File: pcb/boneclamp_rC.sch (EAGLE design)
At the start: 133 parts, among them U1 OPA365AIDBVR, U10 AD5686, U11 LM2663, U12 MAX1735, U13 TLV70245, U14 REF5040, U15 AD8032, U16 24C, U2 OPA365AIDBVR, U3 OPA365AIDBVR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

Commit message: Working on mixed signal ICs/
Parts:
- added SJ2: (no value), jumper:SJ
- R36: device boneclamp:TRIM_US- -> boneclamp:TRIM_US-M84W
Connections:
- new net N$28: BB1.GND@7, SJ2.1
- new net PE: SJ2.2
- net ADC_SPI0: now also BB1.GPIO1_1
- net ADC_SPI1: now also BB1.GPIO1_4
- net ADC_SPI2: now also BB1.GPIO1_5
- net ADC_SPI3: now also BB1.GPIO1_30
- net ADC_SPI4: now also BB1.GPIO1_31
- net DAC_SPI0: now also BB1.GPIO1_14
- net DAC_SPI1: now also BB1.GPIO1_15
- net DAC_SPI2: now also BB1.GPIO1_12
- net DGND: no longer RESET.S
- net ~RST: no longer RESET.P
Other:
- moved on the sheet: R24, R25
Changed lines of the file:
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@@
 <part name="SUPPLY21" library="supply2" deviceset="AGND" device=""/>
 <part name="VBIAS" library="testpad" deviceset="TP" device="B1,27"/>
-<part name="R36" library="boneclamp" deviceset="TRIM_US-" device="" value="10k"/>
+<part name="R36" library="boneclamp" deviceset="TRIM_US-" device="M84W" value="10k"/>
 <part name="C42" library="rcl" deviceset="C-EU" device="C0603" value="0.1uF"/>
 <part name="SUPPLY13" library="supply2" deviceset="AGND" device=""/>
@@
 <part name="R14" library="rcl" deviceset="R-US_" device="R0603" value="10"/>
 <part name="C38" library="rcl" deviceset="C-US" device="C1206" value="4.7uF"/>
+<part name="SJ2" library="jumper" deviceset="SJ" device=""/>
 </parts>
 <sheets>
@@
 <instances>
 <instance part="BB1" gate="G$1" x="-35.56" y="48.26"/>
-<instance part="DGND2" gate="PE" x="2.54" y="-20.32"/>
+<instance part="DGND2" gate="PE" x="-86.36" y="104.14" rot="MR0"/>
 <instance part="SUPPLY8" gate="G$1" x="17.78" y="33.02"/>
 <instance part="A_I/O" gate="G$1" x="53.34" y="30.48"/>
@@
 <instance part="RESET" gate="G$1" x="81.28" y="7.62" rot="R270"/>
 <instance part="DGND10" gate="PE" x="93.98" y="0"/>
+<instance part="SJ2" gate="1" x="-78.74" y="109.22" rot="MR0"/>
 </instances>
 <busses>
@@
 <net name="DGND" class="0">
 <segment>
-<pinref part="RESET" gate="G$1" pin="S"/>
 <pinref part="RESET" gate="G$1" pin="S1"/>
-<wire x1="86.36" y1="7.62" x2="86.36" y2="5.08" width="0.1524" layer="91"/>
 <wire x1="86.36" y1="5.08" x2="93.98" y2="5.08" width="0.1524" layer="91"/>
-<junction x="86.36" y="5.08"/>
 <pinref part="DGND10" gate="PE" pin="PE"/>
 <wire x1="93.98" y1="2.54" x2="93.98" y2="5.08" width="0.1524" layer="91"/>
@@
 <label x="27.94" y="73.66" size="1.778" layer="95"/>
 </segment>
+<segment>
+<pinref part="BB1" gate="G$1" pin="GPIO1_1"/>
+<wire x1="-7.62" y1="81.28" x2="10.16" y2="81.28" width="0.1524" layer="91"/>
+<wire x1="-7.62" y1="81.28" x2="10.16" y2="81.28" width="0.1524" layer="91"/>
+</segment>
 </net>
 <net name="ADC_SPI1" class="0">
@@
 <label x="27.94" y="71.12" size="1.778" layer="95"/>
 </segment>
+<segment>
+<pinref part="BB1" gate="G$1" pin="GPIO1_4"/>
+<wire x1="-63.5" y1="81.28" x2="-81.28" y2="81.28" width="0.1524" layer="91"/>
+</segment>
 </net>
 <net name="ADC_SPI2" class="0">
@@
 <label x="27.94" y="68.58" size="1.778" layer="95"/>
 </segment>
+<segment>
+<pinref part="BB1" gate="G$1" pin="GPIO1_5"/>
+<wire x1="-7.62" y1="83.82" x2="10.16" y2="83.82" width="0.1524" layer="91"/>
+</segment>
 </net>
 <net name="ADC_SPI3" class="0">
@@
 <label x="27.94" y="66.04" size="1.778" layer="95"/>
 </segment>
+<segment>
+<pinref part="BB1" gate="G$1" pin="GPIO1_30"/>
+<wire x1="-63.5" y1="83.82" x2="-81.28" y2="83.82" width="0.1524" layer="91"/>
+</segment>
 </net>
 <net name="ADC_SPI4" class="0">
@@
 <label x="27.94" y="63.5" size="1.778" layer="95"/>
 </segment>
+<segment>
+<pinref part="BB1" gate="G$1" pin="GPIO1_31"/>
+<wire x1="-7.62" y1="86.36" x2="10.16" y2="86.36" width="0.1524" layer="91"/>
+</segment>
 </net>
 <net name="DAC_SPI0" class="0">
@@
 <label x="76.2" y="73.66" size="1.778" layer="95"/>
 </segment>
+<segment>
+<pinref part="BB1" gate="G$1" pin="GPIO1_14"/>
+<wire x1="-7.62" y1="91.44" x2="10.16" y2="91.44" width="0.1524" layer="91"/>
+</segment>
 </net>
 <net name="DAC_SPI1" class="0">
@@
 <label x="76.2" y="71.12" size="1.778" layer="95"/>
 </segment>
+<segment>
+<pinref part="BB1" gate="G$1" pin="GPIO1_15"/>
+<wire x1="-63.5" y1="91.44" x2="-81.28" y2="91.44" width="0.1524" layer="91"/>
+</segment>
 </net>
 <net name="DAC_SPI2" class="0">
@@
 <label x="76.2" y="68.58" size="1.778" layer="95"/>
 </segment>
+<segment>
+<pinref part="BB1" gate="G$1" pin="GPIO1_12"/>
+<wire x1="-7.62" y1="96.52" x2="10.16" y2="96.52" width="0.1524" layer="91"/>
+</segment>
 </net>
 <net name="~RST" class="0">
 <segment>
-<pinref part="RESET" gate="G$1" pin="P"/>
 <pinref part="RESET" gate="G$1" pin="P1"/>
-<wire x1="76.2" y1="7.62" x2="76.2" y2="5.08" width="0.1524" layer="91"/>
 <wire x1="76.2" y1="5.08" x2="66.04" y2="5.08" width="0.1524" layer="91"/>
-<junction x="76.2" y="5.08"/>
 <label x="66.04" y="5.08" size="1.778" layer="95"/>
 </segment>
@@
 <wire x1="35.56" y1="5.08" x2="50.8" y2="5.08" width="0.1524" layer="91"/>
 <label x="35.56" y="5.08" size="1.778" layer="95"/>
+</segment>
+</net>
+<net name="N$28" class="0">
+<segment>
+<pinref part="BB1" gate="G$1" pin="GND@7"/>
+<wire x1="-63.5" y1="109.22" x2="-73.66" y2="109.22" width="0.1524" layer="91"/>
+<pinref part="SJ2" gate="1" pin="1"/>
+</segment>
+</net>
+<net name="PE" class="0">
+<segment>
+<pinref part="DGND2" gate="PE" pin="PE"/>
+<wire x1="-86.36" y1="109.22" x2="-86.36" y2="106.68" width="0.1524" layer="91"/>
+<pinref part="SJ2" gate="1" pin="2"/>
+<wire x1="-83.82" y1="109.22" x2="-86.36" y2="109.22" width="0.1524" layer="91"/>
 </segment>
 </net>
@@
 <instance part="C24" gate="G$1" x="25.4" y="10.16"/>
 <instance part="SUPPLY7" gate="G$1" x="25.4" y="-2.54"/>
-<instance part="R24" gate="G$1" x="-50.8" y="-20.32" rot="R270"/>
-<instance part="R25" gate="G$1" x="-43.18" y="-20.32" rot="R270"/>
+<instance part="R24" gate="G$1" x="-50.8" y="12.7" rot="MR90"/>
+<instance part="R25" gate="G$1" x="-43.18" y="12.7" rot="MR90"/>
 <instance part="U6" gate="A" x="0" y="144.78"/>
 <instance part="R15" gate="G$1" x="-40.64" y="139.7" rot="R180"/>
@@
 <segment>
 <pinref part="R24" gate="G$1" pin="2"/>
-<wire x1="-50.8" y1="-25.4" x2="-50.8" y2="-33.02" width="0.1524" layer="91"/>
+<wire x1="-50.8" y1="17.78" x2="-50.8" y2="22.86" width="0.1524" layer="91"/>
 <pinref part="R25" gate="G$1" pin="2"/>
-<wire x1="-43.18" y1="-25.4" x2="-43.18" y2="-33.02" width="0.1524" layer="91"/>
-<wire x1="-50.8" y1="-33.02" x2="-43.18" y2="-33.02" width="0.1524" layer="91"/>
-<wire x1="-43.18" y1="-33.02" x2="-43.18" y2="-43.18" width="0.1524" layer="91"/>
-<junction x="-43.18" y="-33.02"/>
-<wire x1="-43.18" y1="-43.18" x2="-55.88" y2="-43.18" width="0.1524" layer="91"/>
-<label x="-55.88" y="-43.18" size="1.778" layer="95"/>
+<wire x1="-43.18" y1="17.78" x2="-43.18" y2="22.86" width="0.1524" layer="91"/>
+<wire x1="-50.8" y1="22.86" x2="-43.18" y2="22.86" width="0.1524" layer="91"/>
+<wire x1="-50.8" y1="22.86" x2="-88.9" y2="22.86" width="0.1524" layer="91"/>
+<junction x="-50.8" y="22.86"/>
+<label x="-88.9" y="22.86" size="1.778" layer="95"/>
 </segment>
 </net>
@@
 <pinref part="R24" gate="G$1" pin="1"/>
 <wire x1="-50.8" y1="2.54" x2="-88.9" y2="2.54" width="0.1524" layer="91"/>
-<wire x1="-50.8" y1="-15.24" x2="-50.8" y2="2.54" width="0.1524" layer="91"/>
+<wire x1="-50.8" y1="7.62" x2="-50.8" y2="2.54" width="0.1524" layer="91"/>
 <junction x="-50.8" y="2.54"/>
 <label x="-88.9" y="2.54" size="1.778" layer="95"/>
@@
 <segment>
 <pinref part="R25" gate="G$1" pin="1"/>
-<wire x1="-43.18" y1="-15.24" x2="-43.18" y2="0" width="0.1524" layer="91"/>
+<wire x1="-43.18" y1="7.62" x2="-43.18" y2="0" width="0.1524" layer="91"/>
 <pinref part="U10" gate="G$1" pin="LDAC*"/>
 <wire x1="-88.9" y1="0" x2="-43.18" y2="0" width="0.1524" layer="91"/>

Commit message: Fixed the ground planes.
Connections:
- removed net N$28: BB1.GND@7, SJ2.1
- removed net PE: SJ2.2
- new net N$8: BB1.GND@2, SJ2.1
- net AGND: now also BB1.GND@1; no longer BB1.GND@2
- net DGND: now also SJ2.2
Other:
- moved on the sheet: SJ2
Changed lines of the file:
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@@
 <instances>
 <instance part="BB1" gate="G$1" x="-35.56" y="48.26"/>
-<instance part="DGND2" gate="PE" x="-86.36" y="104.14" rot="MR0"/>
-<instance part="SUPPLY8" gate="G$1" x="17.78" y="33.02"/>
+<instance part="DGND2" gate="PE" x="17.78" y="38.1"/>
+<instance part="SUPPLY8" gate="G$1" x="-88.9" y="38.1"/>
 <instance part="A_I/O" gate="G$1" x="53.34" y="30.48"/>
 <instance part="PWR_EXT" gate="A" x="53.34" y="7.62"/>
 <instance part="RESET" gate="G$1" x="81.28" y="7.62" rot="R270"/>
 <instance part="DGND10" gate="PE" x="93.98" y="0"/>
-<instance part="SJ2" gate="1" x="-78.74" y="109.22" rot="MR0"/>
+<instance part="SJ2" gate="1" x="10.16" y="43.18"/>
 </instances>
 <busses>
@@
 <wire x1="93.98" y1="2.54" x2="93.98" y2="5.08" width="0.1524" layer="91"/>
 </segment>
+<segment>
+<pinref part="DGND2" gate="PE" pin="PE"/>
+<wire x1="17.78" y1="43.18" x2="17.78" y2="40.64" width="0.1524" layer="91"/>
+<pinref part="SJ2" gate="1" pin="2"/>
+<wire x1="15.24" y1="43.18" x2="17.78" y2="43.18" width="0.1524" layer="91"/>
+</segment>
 </net>
 <net name="AGND" class="0">
-<segment>
-<wire x1="17.78" y1="43.18" x2="17.78" y2="35.56" width="0.1524" layer="91"/>
-<pinref part="SUPPLY8" gate="G$1" pin="AGND"/>
-<pinref part="BB1" gate="G$1" pin="GND@2"/>
-<wire x1="-7.62" y1="43.18" x2="17.78" y2="43.18" width="0.1524" layer="91"/>
-</segment>
 <segment>
 <wire x1="35.56" y1="7.62" x2="50.8" y2="7.62" width="0.1524" layer="91"/>
@@
 <label x="66.04" y="33.02" size="1.778" layer="95"/>
 </segment>
+<segment>
+<pinref part="SUPPLY8" gate="G$1" pin="AGND"/>
+<wire x1="-88.9" y1="40.64" x2="-88.9" y2="43.18" width="0.1524" layer="91"/>
+<pinref part="BB1" gate="G$1" pin="GND@1"/>
+<wire x1="-88.9" y1="43.18" x2="-63.5" y2="43.18" width="0.1524" layer="91"/>
+</segment>
 </net>
 <net name="VDD_5V" class="0">
@@
 </segment>
 </net>
-<net name="N$28" class="0">
-<segment>
-<pinref part="BB1" gate="G$1" pin="GND@7"/>
-<wire x1="-63.5" y1="109.22" x2="-73.66" y2="109.22" width="0.1524" layer="91"/>
+<net name="N$8" class="0">
+<segment>
 <pinref part="SJ2" gate="1" pin="1"/>
-</segment>
-</net>
-<net name="PE" class="0">
-<segment>
-<pinref part="DGND2" gate="PE" pin="PE"/>
-<wire x1="-86.36" y1="109.22" x2="-86.36" y2="106.68" width="0.1524" layer="91"/>
-<pinref part="SJ2" gate="1" pin="2"/>
-<wire x1="-83.82" y1="109.22" x2="-86.36" y2="109.22" width="0.1524" layer="91"/>
-</segment>
-</net>
+<pinref part="BB1" gate="G$1" pin="GND@2"/>
+<wire x1="5.08" y1="43.18" x2="-7.62" y2="43.18" width="0.1524" layer="91"/>
+</segment>
+</net>

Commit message: Routed the SPI buses.
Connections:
- net ADC_SPI0: now also BB1.GPIO1_4; no longer BB1.GPIO1_1
- net ADC_SPI1: now also BB1.GPIO1_1; no longer BB1.GPIO1_4
- net ADC_SPI2: now also BB1.GPIO1_30; no longer BB1.GPIO1_5
- net ADC_SPI3: now also BB1.GPIO1_5; no longer BB1.GPIO1_30
- net DAC_SPI0: now also BB1.GPIO1_15; no longer BB1.GPIO1_14
- net DAC_SPI1: now also BB1.GPIO1_14; no longer BB1.GPIO1_15
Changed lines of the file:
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@@
 </segment>
 <segment>
-<pinref part="BB1" gate="G$1" pin="GPIO1_1"/>
-<wire x1="-7.62" y1="81.28" x2="10.16" y2="81.28" width="0.1524" layer="91"/>
-<wire x1="-7.62" y1="81.28" x2="10.16" y2="81.28" width="0.1524" layer="91"/>
+<pinref part="BB1" gate="G$1" pin="GPIO1_4"/>
+<wire x1="-63.5" y1="81.28" x2="-81.28" y2="81.28" width="0.1524" layer="91"/>
 </segment>
 </net>
@@
 </segment>
 <segment>
-<pinref part="BB1" gate="G$1" pin="GPIO1_4"/>
-<wire x1="-63.5" y1="81.28" x2="-81.28" y2="81.28" width="0.1524" layer="91"/>
+<pinref part="BB1" gate="G$1" pin="GPIO1_1"/>
+<wire x1="-7.62" y1="81.28" x2="10.16" y2="81.28" width="0.1524" layer="91"/>
+<wire x1="-7.62" y1="81.28" x2="10.16" y2="81.28" width="0.1524" layer="91"/>
 </segment>
 </net>
@@
 </segment>
 <segment>
-<pinref part="BB1" gate="G$1" pin="GPIO1_5"/>
-<wire x1="-7.62" y1="83.82" x2="10.16" y2="83.82" width="0.1524" layer="91"/>
+<pinref part="BB1" gate="G$1" pin="GPIO1_30"/>
+<wire x1="-63.5" y1="83.82" x2="-81.28" y2="83.82" width="0.1524" layer="91"/>
 </segment>
 </net>
@@
 </segment>
 <segment>
-<pinref part="BB1" gate="G$1" pin="GPIO1_30"/>
-<wire x1="-63.5" y1="83.82" x2="-81.28" y2="83.82" width="0.1524" layer="91"/>
+<pinref part="BB1" gate="G$1" pin="GPIO1_5"/>
+<wire x1="-7.62" y1="83.82" x2="10.16" y2="83.82" width="0.1524" layer="91"/>
 </segment>
 </net>
@@
 </segment>
 <segment>
-<pinref part="BB1" gate="G$1" pin="GPIO1_14"/>
-<wire x1="-7.62" y1="91.44" x2="10.16" y2="91.44" width="0.1524" layer="91"/>
+<pinref part="BB1" gate="G$1" pin="GPIO1_15"/>
+<wire x1="-63.5" y1="91.44" x2="-81.28" y2="91.44" width="0.1524" layer="91"/>
 </segment>
 </net>
@@
 </segment>
 <segment>
-<pinref part="BB1" gate="G$1" pin="GPIO1_15"/>
-<wire x1="-63.5" y1="91.44" x2="-81.28" y2="91.44" width="0.1524" layer="91"/>
+<pinref part="BB1" gate="G$1" pin="GPIO1_14"/>
+<wire x1="-7.62" y1="91.44" x2="10.16" y2="91.44" width="0.1524" layer="91"/>
 </segment>
 </net>

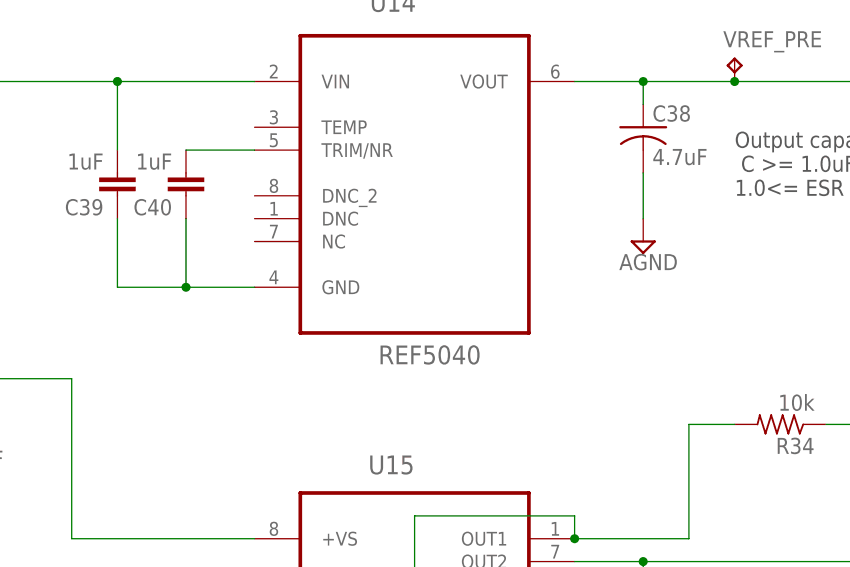
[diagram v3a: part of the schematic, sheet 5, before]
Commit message: Started to route IC groups together.
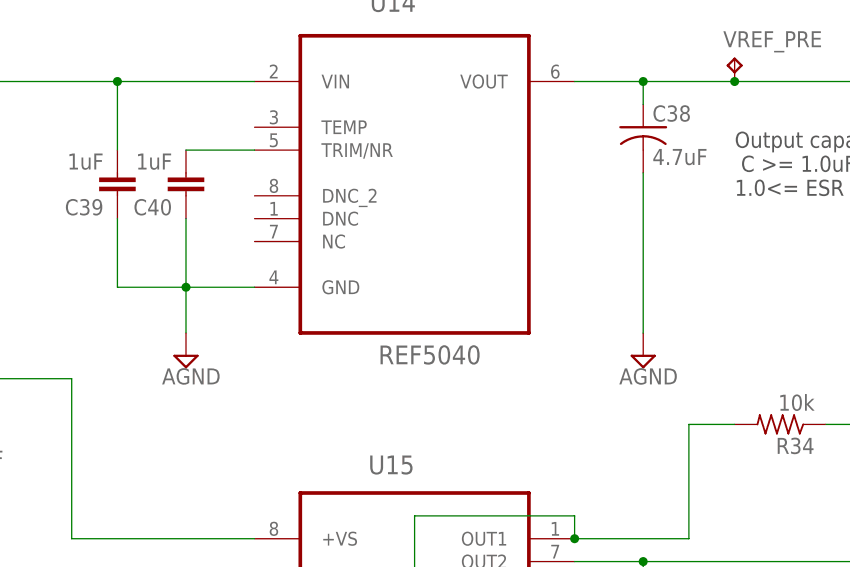
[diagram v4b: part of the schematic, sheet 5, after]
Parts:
- added C46: 1uF, rcl:C-EUC0603
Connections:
- removed net N$12: C39.1, C40.1, U14.GND
- net +4.5V: now also C46.1
- net -4.5V: now also C46.2
- net ADC_SPI3: now also BB1.GPIO1_31; no longer BB1.GPIO1_5
- net ADC_SPI4: now also BB1.GPIO1_5; no longer BB1.GPIO1_31
- net AGND: now also C39.1, C40.1, U14.GND
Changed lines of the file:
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@@
 <part name="C38" library="rcl" deviceset="C-US" device="C1206" value="4.7uF"/>
 <part name="SJ2" library="jumper" deviceset="SJ" device=""/>
+<part name="C46" library="rcl" deviceset="C-EU" device="C0603" value="1uF"/>
+<part name="SUPPLY38" library="supply2" deviceset="AGND" device=""/>
 </parts>
 <sheets>
@@
 </segment>
 <segment>
+<pinref part="BB1" gate="G$1" pin="GPIO1_31"/>
+<wire x1="-7.62" y1="86.36" x2="10.16" y2="86.36" width="0.1524" layer="91"/>
+</segment>
+</net>
+<net name="ADC_SPI4" class="0">
+<segment>
+<wire x1="27.94" y1="63.5" x2="40.64" y2="63.5" width="0.1524" layer="91"/>
+<label x="27.94" y="63.5" size="1.778" layer="95"/>
+</segment>
+<segment>
 <pinref part="BB1" gate="G$1" pin="GPIO1_5"/>
 <wire x1="-7.62" y1="83.82" x2="10.16" y2="83.82" width="0.1524" layer="91"/>
-</segment>
-</net>
-<net name="ADC_SPI4" class="0">
-<segment>
-<wire x1="27.94" y1="63.5" x2="40.64" y2="63.5" width="0.1524" layer="91"/>
-<label x="27.94" y="63.5" size="1.778" layer="95"/>
-</segment>
-<segment>
-<pinref part="BB1" gate="G$1" pin="GPIO1_31"/>
-<wire x1="-7.62" y1="86.36" x2="10.16" y2="86.36" width="0.1524" layer="91"/>
 </segment>
 </net>
@@
 <instance part="EXT_PWR" gate="G$1" x="96.52" y="-68.58" rot="R90"/>
 <instance part="SUPPLY34" gate="G$1" x="106.68" y="-71.12"/>
+<instance part="C46" gate="G$1" x="88.9" y="10.16"/>
 </instances>
 <busses>
@@
 <label x="68.58" y="-55.88" size="1.778" layer="95"/>
 <wire x1="81.28" y1="-55.88" x2="68.58" y2="-55.88" width="0.1524" layer="91"/>
+</segment>
+<segment>
+<pinref part="C46" gate="G$1" pin="1"/>
+<wire x1="78.74" y1="12.7" x2="88.9" y2="12.7" width="0.1524" layer="91"/>
+<wire x1="88.9" y1="12.7" x2="101.6" y2="12.7" width="0.1524" layer="91"/>
+<junction x="88.9" y="12.7"/>
+<label x="78.74" y="12.7" size="1.778" layer="95"/>
 </segment>
 </net>
@@
 <junction x="30.48" y="-10.16"/>
 </segment>
+<segment>
+<pinref part="C46" gate="G$1" pin="2"/>
+<wire x1="88.9" y1="5.08" x2="78.74" y2="5.08" width="0.1524" layer="91"/>
+<wire x1="88.9" y1="5.08" x2="101.6" y2="5.08" width="0.1524" layer="91"/>
+<junction x="88.9" y="5.08"/>
+<label x="78.74" y="5.08" size="1.778" layer="95"/>
+</segment>
 </net>
 <net name="N$5" class="0">
@@
 <instance part="C39" gate="G$1" x="-33.02" y="-5.08" rot="R180"/>
 <instance part="C40" gate="G$1" x="-25.4" y="-5.08" rot="R180"/>
-<instance part="SUPPLY22" gate="G$1" x="25.4" y="-10.16"/>
+<instance part="SUPPLY22" gate="G$1" x="25.4" y="-22.86"/>
 <instance part="VREF_PRE" gate="G$1" x="35.56" y="10.16"/>
 <instance part="U15" gate="A" x="0" y="-50.8"/>
@@
 <instance part="VREF" gate="G$1" x="73.66" y="-27.94"/>
 <instance part="C38" gate="G$1" x="25.4" y="2.54"/>
+<instance part="SUPPLY38" gate="G$1" x="-25.4" y="-22.86"/>
 </instances>
 <busses>
@@
 <net name="AGND" class="0">
 <segment>
-<wire x1="25.4" y1="-7.62" x2="25.4" y2="-2.54" width="0.1524" layer="91"/>
+<wire x1="25.4" y1="-20.32" x2="25.4" y2="-2.54" width="0.1524" layer="91"/>
 <pinref part="SUPPLY22" gate="G$1" pin="AGND"/>
 <pinref part="C38" gate="G$1" pin="2"/>
@@
 <wire x1="50.8" y1="-60.96" x2="50.8" y2="-66.04" width="0.1524" layer="91"/>
 <pinref part="SUPPLY13" gate="G$1" pin="AGND"/>
+</segment>
+<segment>
+<pinref part="C39" gate="G$1" pin="1"/>
+<wire x1="-33.02" y1="-7.62" x2="-33.02" y2="-15.24" width="0.1524" layer="91"/>
+<pinref part="U14" gate="A" pin="GND"/>
+<wire x1="-17.78" y1="-15.24" x2="-25.4" y2="-15.24" width="0.1524" layer="91"/>
+<wire x1="-25.4" y1="-15.24" x2="-33.02" y2="-15.24" width="0.1524" layer="91"/>
+<junction x="-25.4" y="-15.24"/>
+<pinref part="C40" gate="G$1" pin="1"/>
+<wire x1="-25.4" y1="-7.62" x2="-25.4" y2="-15.24" width="0.1524" layer="91"/>
+<pinref part="SUPPLY38" gate="G$1" pin="AGND"/>
+<wire x1="-25.4" y1="-15.24" x2="-25.4" y2="-20.32" width="0.1524" layer="91"/>
 </segment>
 </net>
@@
 <wire x1="-17.78" y1="-60.96" x2="-17.78" y2="-58.42" width="0.1524" layer="91"/>
 <pinref part="R35" gate="G$1" pin="2"/>
-</segment>
-</net>
-<net name="N$12" class="0">
-<segment>
-<pinref part="C39" gate="G$1" pin="1"/>
-<wire x1="-33.02" y1="-7.62" x2="-33.02" y2="-15.24" width="0.1524" layer="91"/>
-<pinref part="U14" gate="A" pin="GND"/>
-<wire x1="-17.78" y1="-15.24" x2="-25.4" y2="-15.24" width="0.1524" layer="91"/>
-<wire x1="-25.4" y1="-15.24" x2="-33.02" y2="-15.24" width="0.1524" layer="91"/>
-<junction x="-25.4" y="-15.24"/>
-<pinref part="C40" gate="G$1" pin="1"/>
-<wire x1="-25.4" y1="-7.62" x2="-25.4" y2="-15.24" width="0.1524" layer="91"/>
 </segment>
 </net>
@@
 </segment>
 <segment>
-<pinref part="U16" gate="G$1" pin="GND"/>
-<wire x1="5.08" y1="2.54" x2="5.08" y2="12.7" width="0.1524" layer="91"/>
-</segment>
-<segment>
 <pinref part="C45" gate="G$1" pin="2"/>
 <wire x1="50.8" y1="20.32" x2="50.8" y2="7.62" width="0.1524" layer="91"/>
 <pinref part="DGND6" gate="PE" pin="PE"/>
+</segment>
+<segment>
+<pinref part="U16" gate="G$1" pin="GND"/>
+<pinref part="DGND4" gate="PE" pin="PE"/>
+<wire x1="5.08" y1="12.7" x2="5.08" y2="7.62" width="0.1524" layer="91"/>
 </segment>
 </net>
@@
 </segment>
 </net>
-<net name="N$16" class="0">
-<segment>
-<wire x1="5.08" y1="2.54" x2="5.08" y2="7.62" width="0.1524" layer="91"/>
-<pinref part="DGND4" gate="PE" pin="PE"/>
-</segment>
-</net>

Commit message: Routing.
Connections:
- new net N$12: R34.2, U15.-IN1, U15.OUT1
- net VREF: no longer R34.2, U15.-IN1, U15.OUT1
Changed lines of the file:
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@@
 <net name="VREF" class="0">
-<segment>
-<wire x1="17.78" y1="-43.18" x2="30.48" y2="-43.18" width="0.1524" layer="91"/>
-<wire x1="0" y1="-40.64" x2="17.78" y2="-40.64" width="0.1524" layer="91"/>
-<wire x1="17.78" y1="-40.64" x2="17.78" y2="-43.18" width="0.1524" layer="91"/>
-<pinref part="U15" gate="A" pin="OUT1"/>
-<junction x="17.78" y="-43.18"/>
-<pinref part="U15" gate="A" pin="-IN1"/>
-<wire x1="-17.78" y1="-50.8" x2="-17.78" y2="-53.34" width="0.1524" layer="91"/>
-<wire x1="-17.78" y1="-53.34" x2="0" y2="-53.34" width="0.1524" layer="91"/>
-<wire x1="0" y1="-53.34" x2="0" y2="-40.64" width="0.1524" layer="91"/>
-<wire x1="30.48" y1="-43.18" x2="30.48" y2="-30.48" width="0.1524" layer="91"/>
-<wire x1="30.48" y1="-30.48" x2="35.56" y2="-30.48" width="0.1524" layer="91"/>
-<pinref part="R34" gate="G$1" pin="2"/>
-</segment>
 <segment>
 <wire x1="-60.96" y1="-68.58" x2="-53.34" y2="-68.58" width="0.1524" layer="91"/>
@@
 </segment>
 </net>
+<net name="N$12" class="0">
+<segment>
+<wire x1="17.78" y1="-43.18" x2="30.48" y2="-43.18" width="0.1524" layer="91"/>
+<wire x1="0" y1="-40.64" x2="17.78" y2="-40.64" width="0.1524" layer="91"/>
+<wire x1="17.78" y1="-40.64" x2="17.78" y2="-43.18" width="0.1524" layer="91"/>
+<pinref part="U15" gate="A" pin="OUT1"/>
+<junction x="17.78" y="-43.18"/>
+<pinref part="U15" gate="A" pin="-IN1"/>
+<wire x1="-17.78" y1="-50.8" x2="-17.78" y2="-53.34" width="0.1524" layer="91"/>
+<wire x1="-17.78" y1="-53.34" x2="0" y2="-53.34" width="0.1524" layer="91"/>
+<wire x1="0" y1="-53.34" x2="0" y2="-40.64" width="0.1524" layer="91"/>
+<pinref part="R34" gate="G$1" pin="2"/>
+<wire x1="30.48" y1="-30.48" x2="35.56" y2="-30.48" width="0.1524" layer="91"/>
+<wire x1="30.48" y1="-43.18" x2="30.48" y2="-30.48" width="0.1524" layer="91"/>
+</segment>
+</net>
